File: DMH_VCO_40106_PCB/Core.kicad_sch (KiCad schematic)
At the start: 48 parts, among them Q1 BC558, Q2 BC548, U1 40106, U2 TL074, U4 TL074

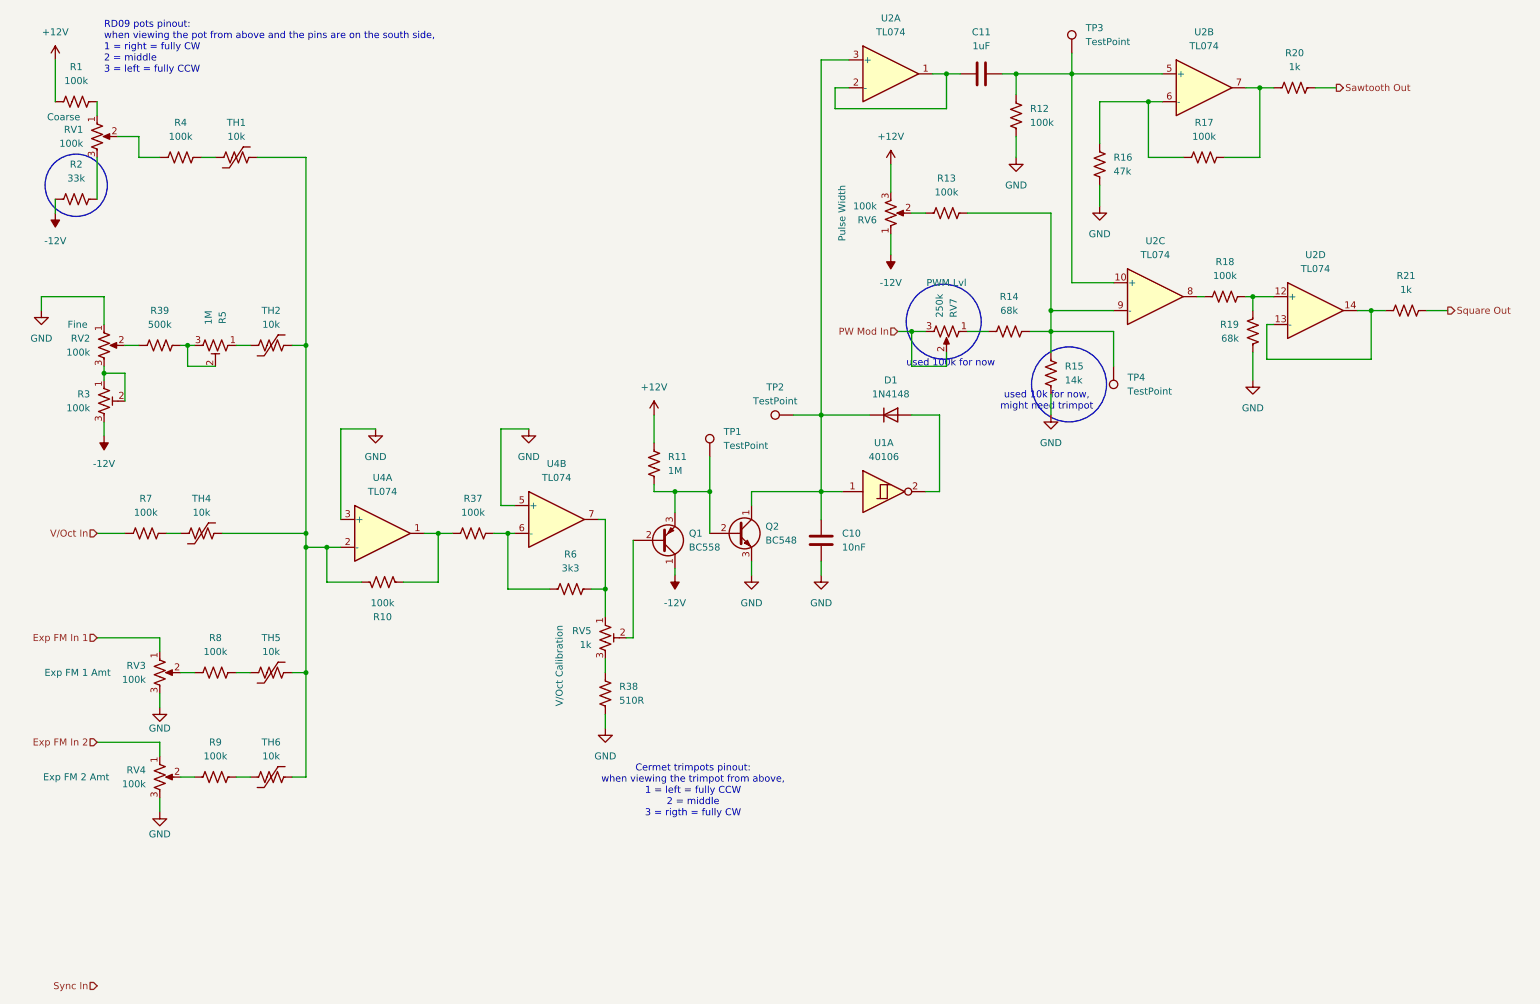
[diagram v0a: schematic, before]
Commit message: Improved fine freq adjustment
And tidied up the CV input summing section
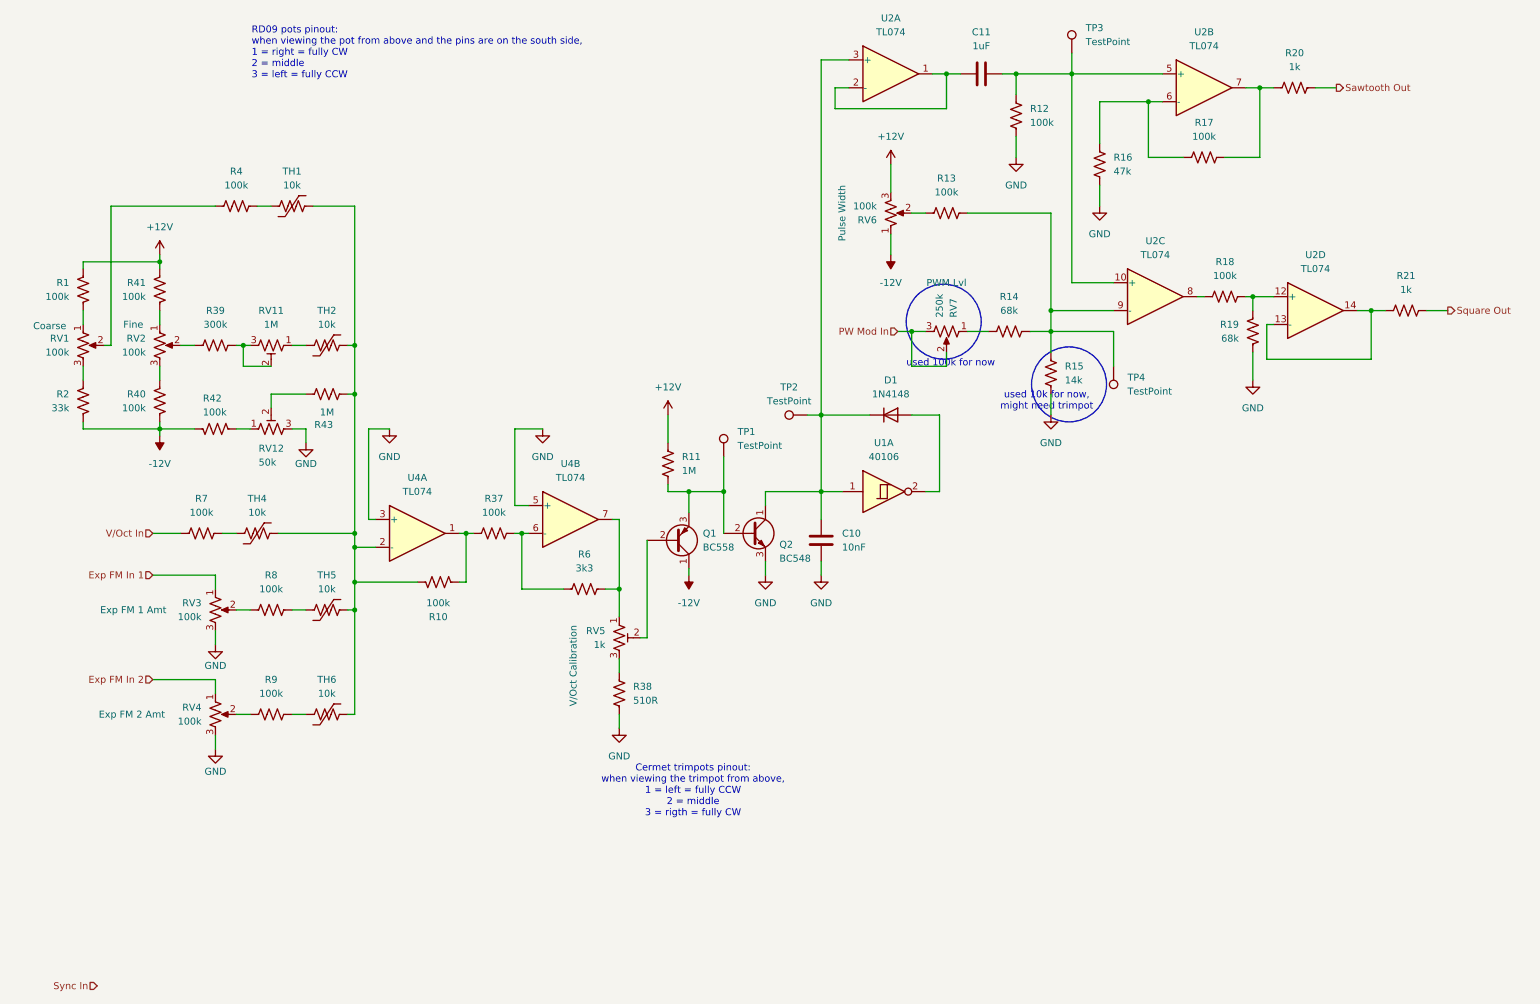
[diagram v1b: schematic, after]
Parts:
- added R40, R41, R42: 100k, Resistor_THT:R_Axial_DIN0204_L3.6mm_D1.6mm_P5.08mm_Horizontal, symbol Device:R_US
- added R43: 1M, Resistor_THT:R_Axial_DIN0204_L3.6mm_D1.6mm_P5.08mm_Horizontal, symbol Device:R_US
- R39: value 500k -> 300k
- RV12: renamed from R3; value 100k -> 50k
- renumbered R5 to RV11
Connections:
- net +12V: now also R1.2, R41.1; no longer R1.1
- net -12V: now also R40.2, R42.2; no longer RV12.3
- net GND: now also RV12.3; no longer RV2.1
- net at R10.1, TH1.2, TH2.2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: now also R43.1
- net at RV1.1: now also R1.1; no longer R1.2
- new net: R42.1, RV12.1
- new net: R40.1, RV2.3
- new net: R41.2, RV2.1
- new net: R43.2, RV12.2
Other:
- moved on the sheet: Q1, Q2, R1, R10, R11, R2, R37, R38, R39, R4, R6, R7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

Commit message: Changed Fine Range trimpot strategy
... in order to allow for range adjustment from -/+13 to -/+0.5 semitones
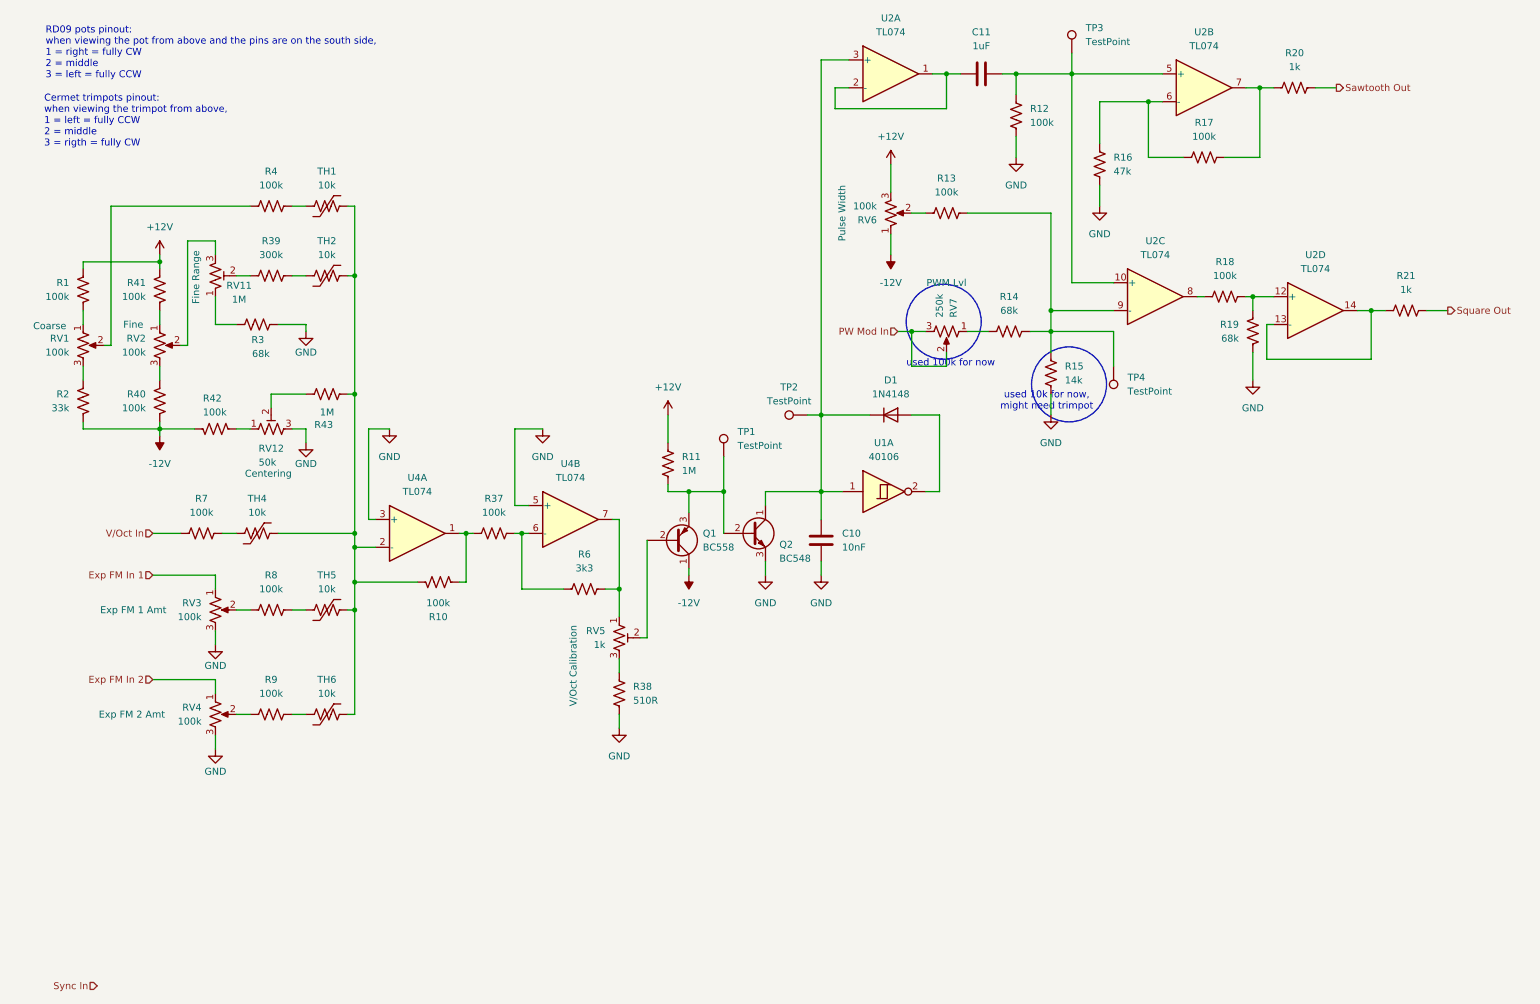
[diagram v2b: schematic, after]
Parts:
- added R3: 68k, Resistor_THT:R_Axial_DIN0204_L3.6mm_D1.6mm_P5.08mm_Horizontal, symbol Device:R_US
- RV12: Function (none) -> Centering
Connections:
- net GND: now also R3.1
- net at RV11.1: now also R3.2; no longer TH2.1
- net at R39.1: now also RV11.2; no longer RV2.2
- new net: RV11.3, RV2.2
- new net: R39.2, TH2.1
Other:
- moved on the sheet: R39, R4, RV11, TH1, TH2

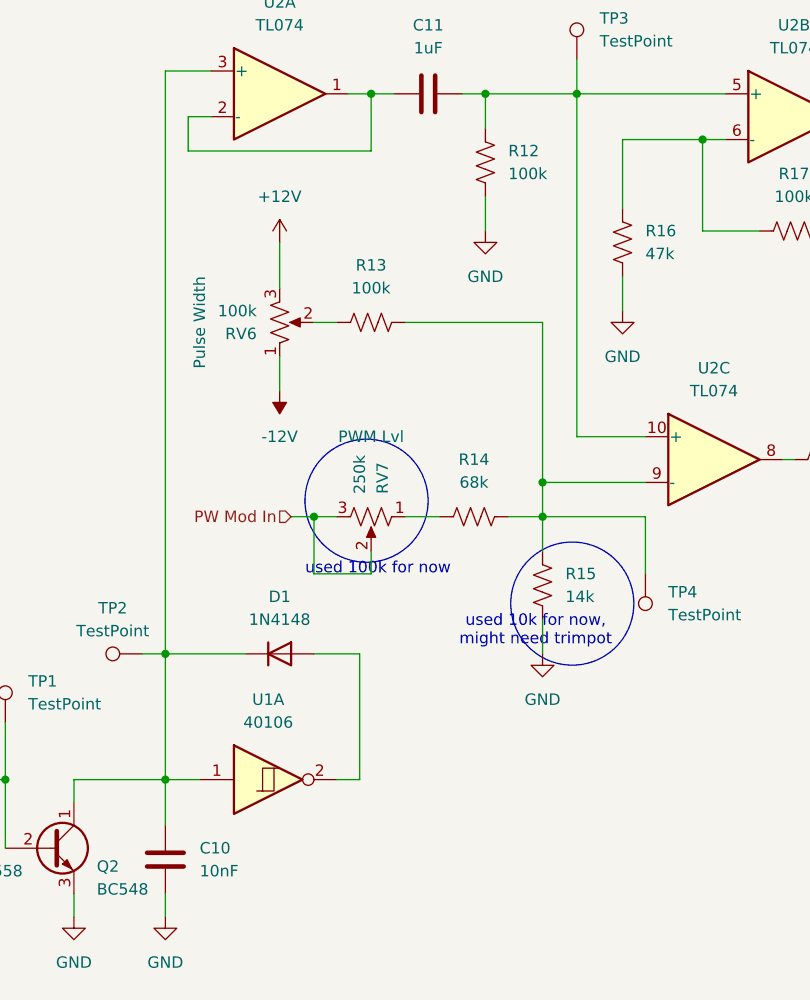
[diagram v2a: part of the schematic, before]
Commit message: Improved PWM part
Made PWM totally killable with 100k "amt" pot.
Added duty cycle range trimpot.
Added duty cycle balancing trimpot.
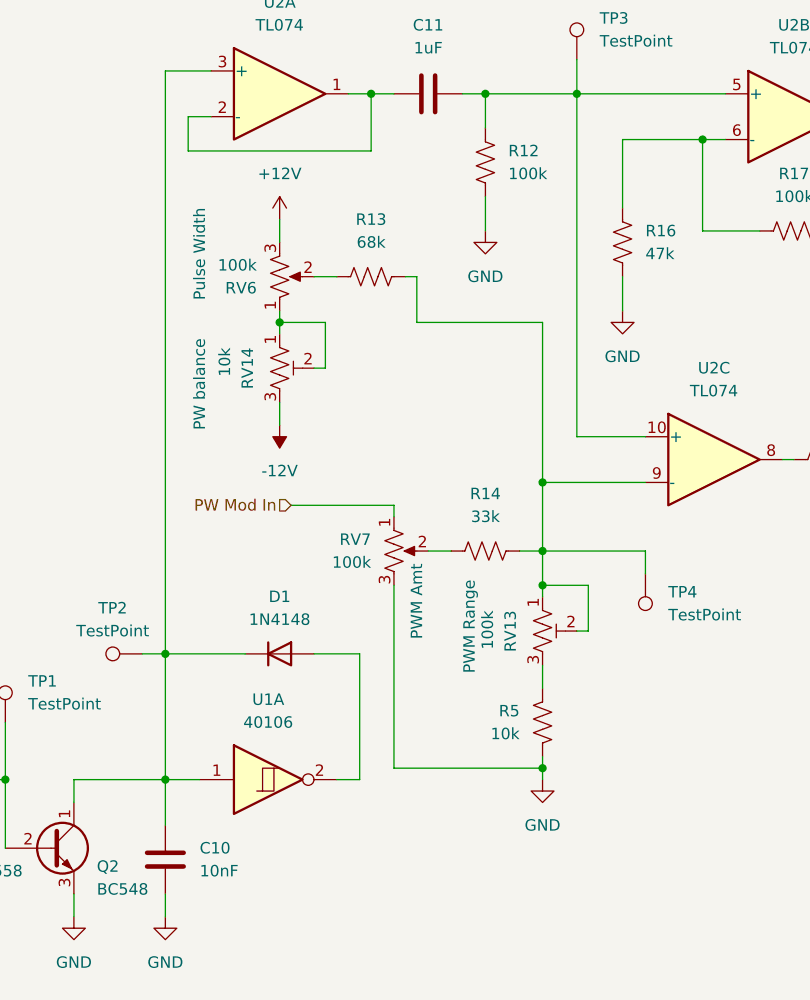
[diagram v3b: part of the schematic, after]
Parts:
- removed R15: 14k, Resistor_THT:R_Axial_DIN0204_L3.6mm_D1.6mm_P5.08mm_Horizontal, symbol Device:R_US
- added R5: 10k, Resistor_THT:R_Axial_DIN0204_L3.6mm_D1.6mm_P5.08mm_Horizontal, symbol Device:R_US
- added RV13: 100k, Resistor_THT:R_Axial_DIN0204_L3.6mm_D1.6mm_P5.08mm_Horizontal, symbol Device:R_Potentiometer_Trim_US
- added RV14: 10k, Resistor_THT:R_Axial_DIN0204_L3.6mm_D1.6mm_P5.08mm_Horizontal, symbol Device:R_Potentiometer_Trim_US
- R13: value 100k -> 68k
- R14: value 68k -> 33k
- RV7: value 250k -> 100k
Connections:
- net -12V: now also RV14.3; no longer RV6.1
- net GND: now also RV7.3, R5.2
- net PW Mod In: now also RV7.1; no longer RV7.2, RV7.3
- net at R13.1, R14.1, TP4.1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: now also RV13.1, RV13.2
- net at R14.2: now also RV7.2; no longer RV7.1
- new net: RV14.1, RV14.2, RV6.1
- new net: R5.1, RV13.3
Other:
- note removed: "used 100k for now"
- note removed: "used 10k for now, might need trimpot"
- moved on the sheet: R13, R14, RV6, RV7

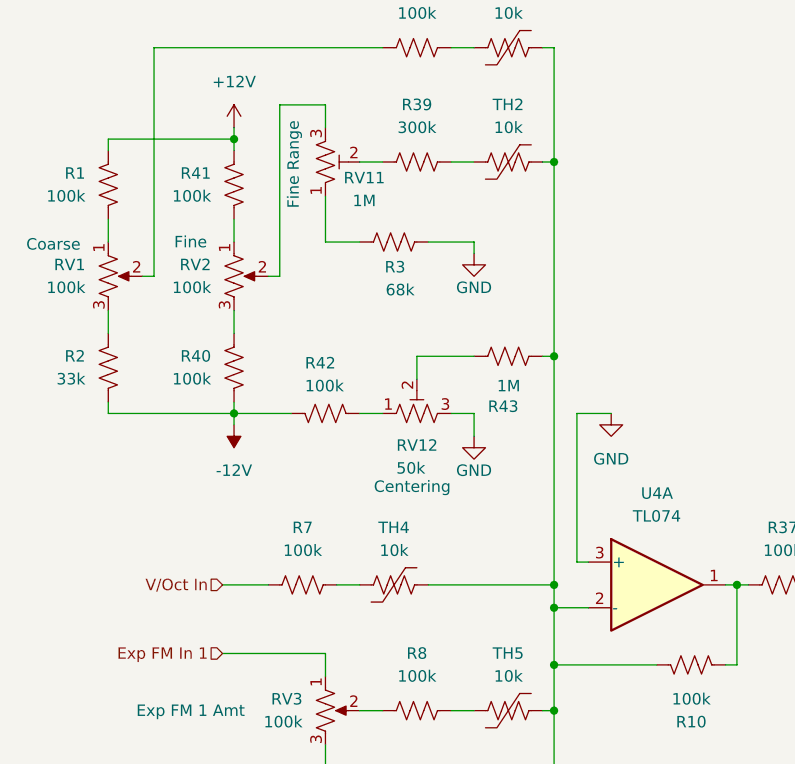
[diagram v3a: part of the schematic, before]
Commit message: Added thermistor to the centring trimpot line
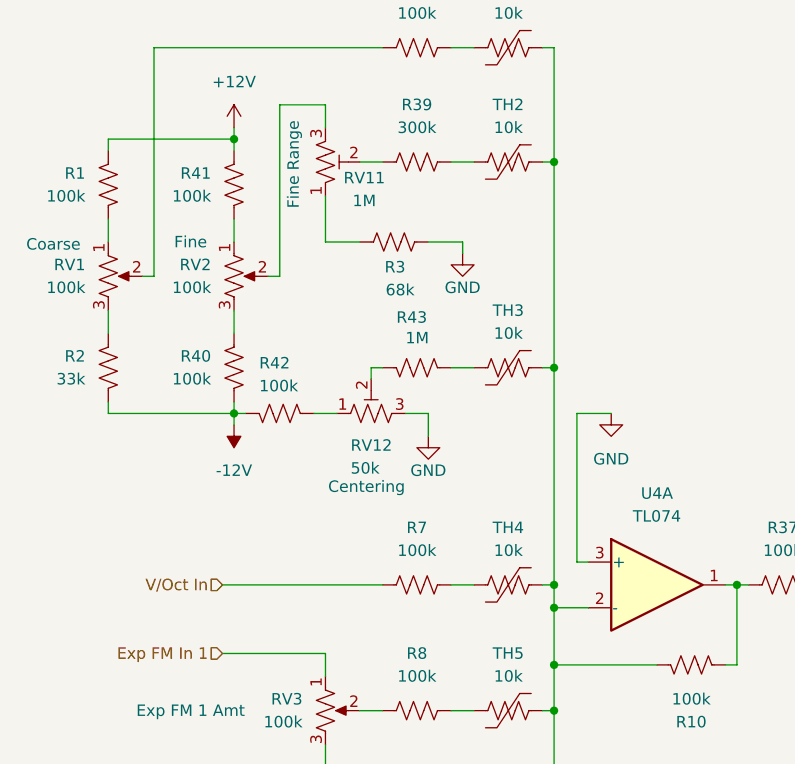
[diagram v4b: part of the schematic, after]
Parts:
- added TH3: 10k, Resistor_THT:R_Axial_DIN0204_L3.6mm_D1.6mm_P5.08mm_Horizontal, symbol Device:Thermistor_US
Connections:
- net at R10.1, TH1.2, TH2.2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: now also TH3.2; no longer R43.1
- new net: R43.1, TH3.1
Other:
- moved on the sheet: R42, R43, R7, RV12, TH4

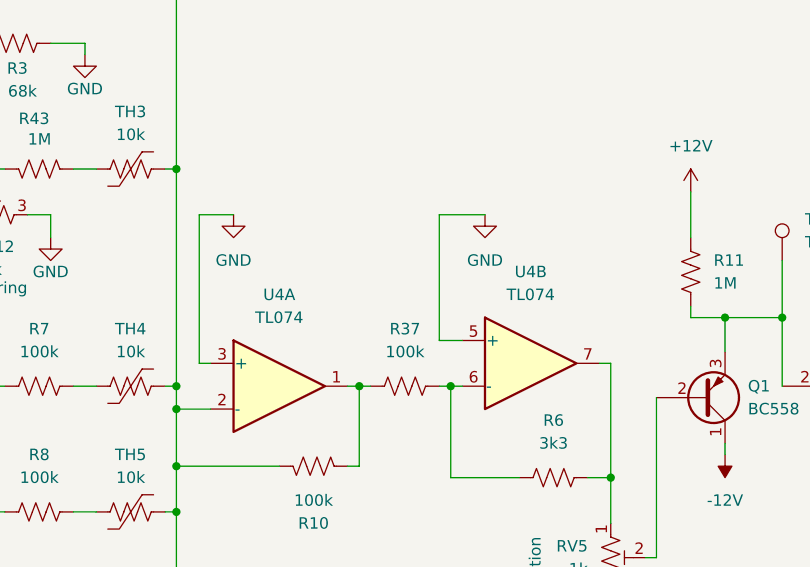
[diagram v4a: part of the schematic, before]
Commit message: Made U3 into TL074 instead of TL072
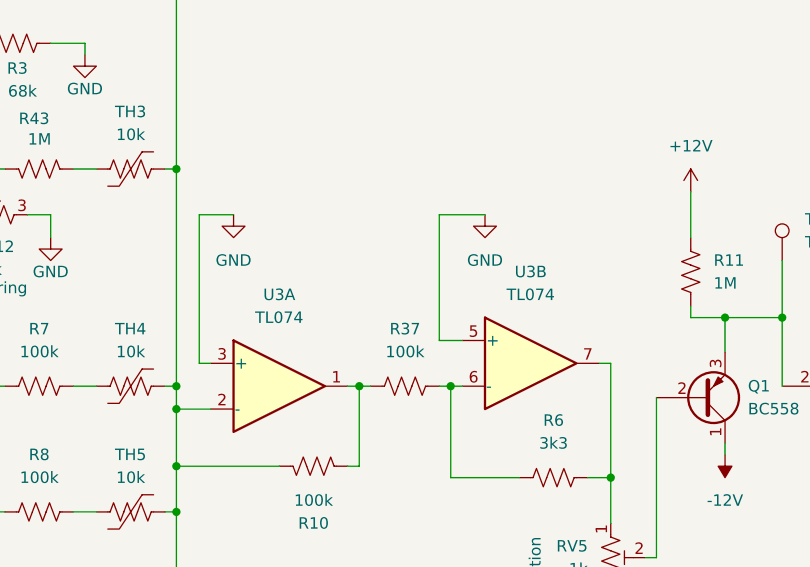
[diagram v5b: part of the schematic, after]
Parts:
- renumbered U4 to U3
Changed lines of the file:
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@@
 		(dnp no)
 		(fields_autoplaced yes)
-		(property "Reference" "U4"
+		(property "Reference" "U3"
 			(at 111.76 95.25 0)
 			(effects
@@
 			(project "DMH_VCO_40106_PCB"
 				(path "/fefed352-c100-4617-bbfb-c55e7427b122/681eb850-910f-47de-ab28-b72b47bdbc38"
-					(reference "U4")
+					(reference "U3")
 					(unit 2)
 				)
@@
 		(dnp no)
 		(fields_autoplaced yes)
-		(property "Reference" "U4"
+		(property "Reference" "U3"
 			(at 83.82 97.79 0)
 			(effects
@@
 			(project "DMH_VCO_40106_PCB"
 				(path "/fefed352-c100-4617-bbfb-c55e7427b122/681eb850-910f-47de-ab28-b72b47bdbc38"
-					(reference "U4")
+					(reference "U3")
 					(unit 1)
 				)
